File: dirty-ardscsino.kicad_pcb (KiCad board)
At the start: 2 copper layers, 70.9 x 82 mm, 18 parts, among them J1 SCSI, J2 171825-4 (Ext. Power), J3 DM3AT-SF-PEJM5, U1 STM32 Bluepill, U2 microSD-Breakout

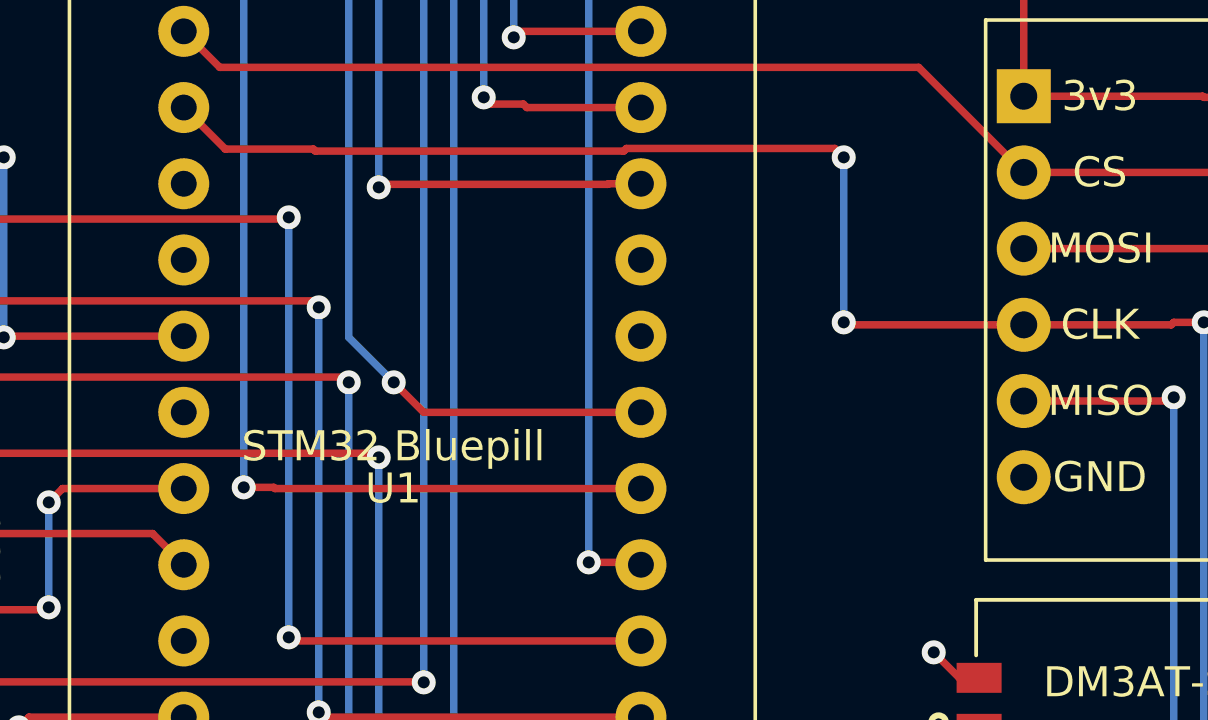
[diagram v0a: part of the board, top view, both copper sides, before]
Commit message: Fix broken MISO/MOSI traces
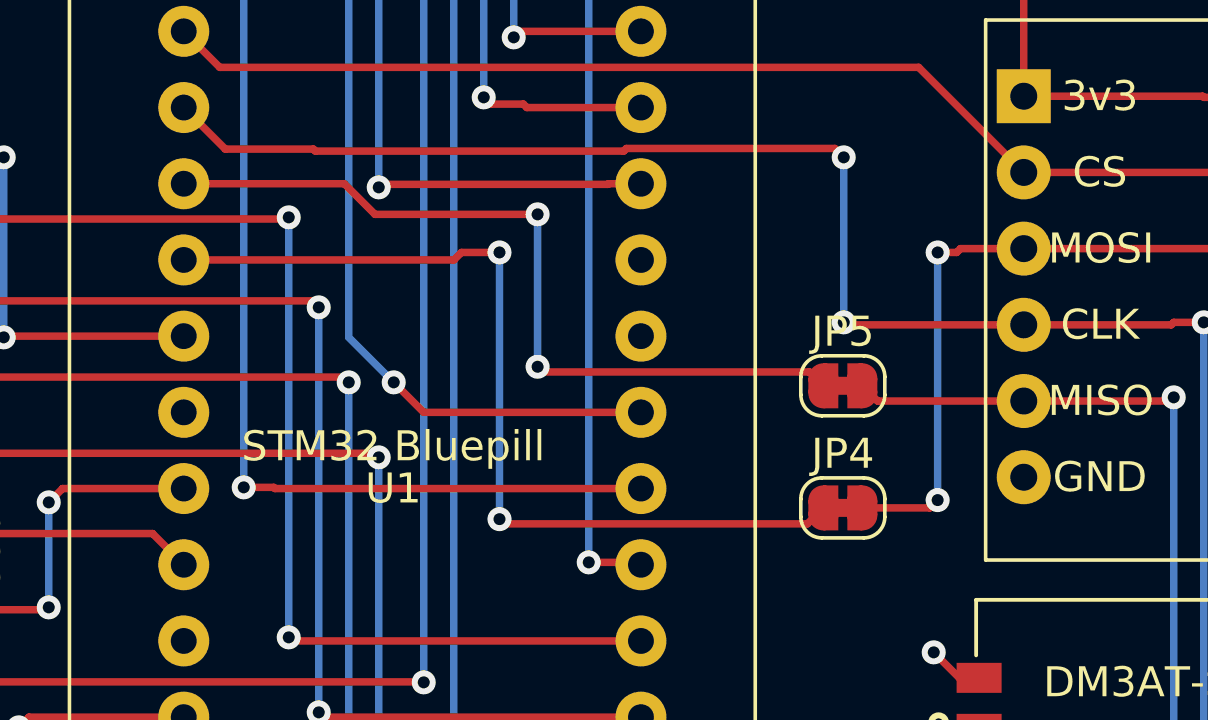
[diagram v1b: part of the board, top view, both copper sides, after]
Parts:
- added JP4: Jumper_2_Bridged, Jumper:SolderJumper-2_P1.3mm_Bridged_RoundedPad1.0x1.5mm, F.Cu at (148.0, 98.7)
- added JP5: Jumper_2_Bridged, Jumper:SolderJumper-2_P1.3mm_Bridged_RoundedPad1.0x1.5mm, F.Cu at (148.0, 94.6)
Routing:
- net /BP_MOSI: track 0.00 -> 30.6 mm, vias 0 -> 2
- net /BP_MISO: track 0.00 -> 27.1 mm, vias 0 -> 2
- net /SD_MOSI: track 35.5 -> 49.3 mm, vias 2 -> 4
- net /SD_MISO: track 28.9 -> 34.5 mm

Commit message: Touch up logo
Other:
- board text added: "leadedsolder.com '25-26 v4"
- board text removed: "leadedsolder.com 2025-26 v4"

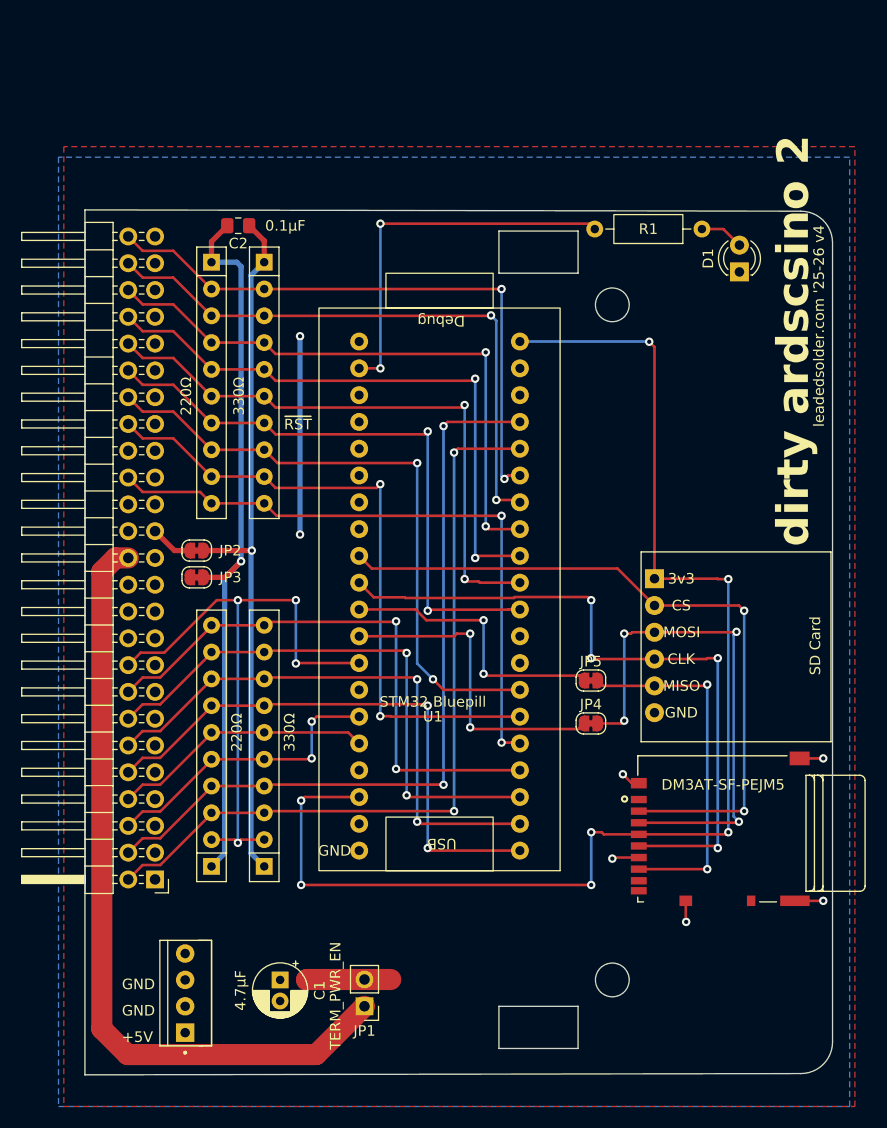
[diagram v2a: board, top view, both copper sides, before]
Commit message: add zener diodes
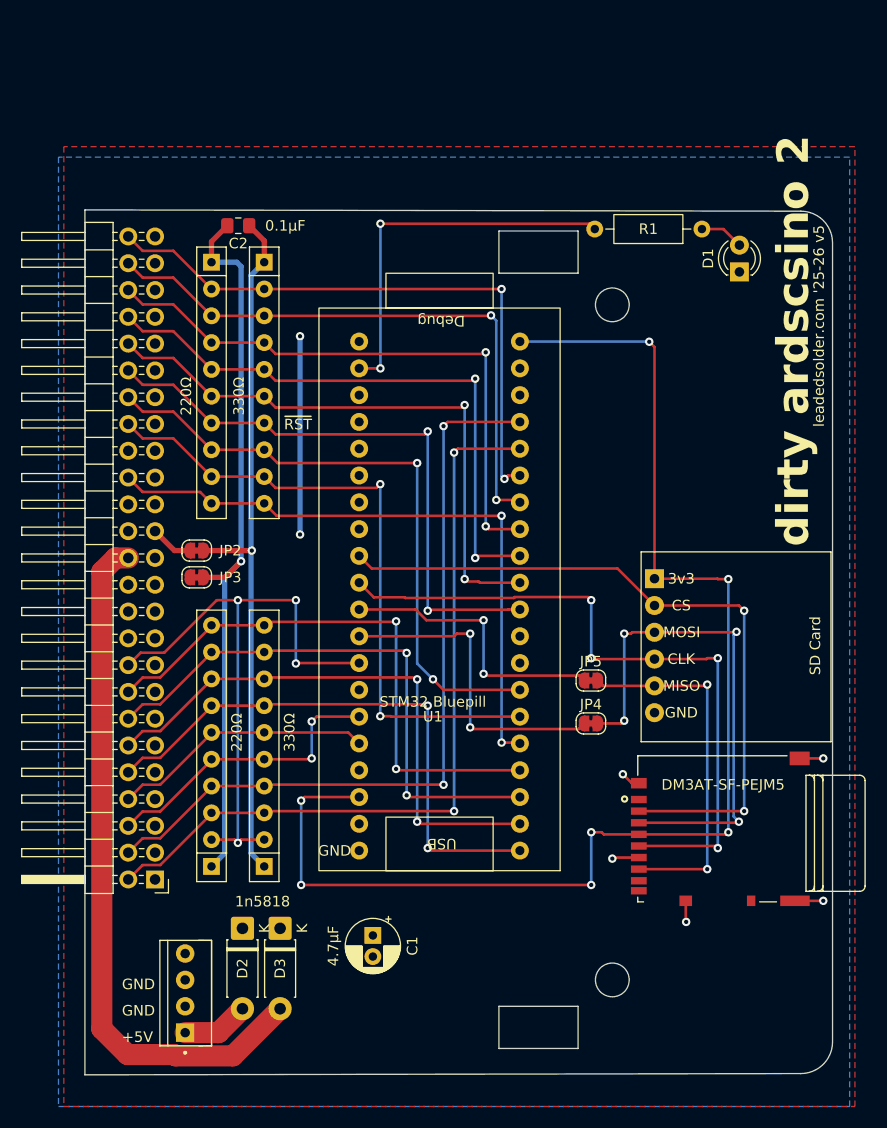
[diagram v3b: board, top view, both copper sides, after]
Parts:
- removed JP1: TERM_PWR_EN, Connector_PinHeader_2.54mm:PinHeader_1x02_P2.54mm_Vertical
- added D2: 1n5818, Diode_THT:D_DO-41_SOD81_P7.62mm_Horizontal, F.Cu at (114.9, 118.1)
- added D3: 1n5818, Diode_THT:D_DO-41_SOD81_P7.62mm_Horizontal, F.Cu at (118.5, 118.1)
- moved C1 9.75 mm to (127.3, 118.8)
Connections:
- J2 pad 1: +5V -> Net-(D2-A)
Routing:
- net +5V: track 26.8 -> 18.8 mm
- net /TERM_POWER: track 74.2 -> 66.2 mm
- net Net-(D2-A): track 0.00 -> 6.37 mm
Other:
- board text added: "leadedsolder.com '25-26 v5"
- board text removed: "leadedsolder.com '25-26 v4"

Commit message: Bump cap to 10µF, label activity LED
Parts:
- C1: value 4.7µF -> 10µF
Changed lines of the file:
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@@
 		(property "Value" "Ext. Activity"
 			(at 1.27 2.96 90)
-			(layer "F.Fab")
+			(layer "F.SilkS")
 			(effects
 				(font
@@
 			)
 		)
-		(property "Value" "4.7µF"
+		(property "Value" "10µF"
 			(at 1 3.75 90)
 			(layer "F.SilkS")
